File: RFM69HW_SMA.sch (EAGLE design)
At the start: 19 parts, among them U1 RFM69W, U2 MCP1701, X1 ANT

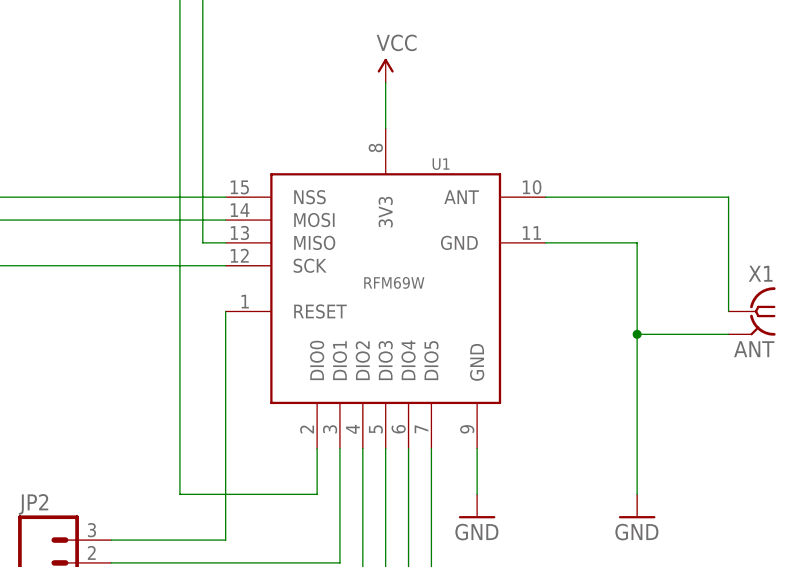
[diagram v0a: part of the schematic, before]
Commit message: Slight relayout
Re-layout. Break out all I/O pins. Use RFM69HW variant (same pinout).
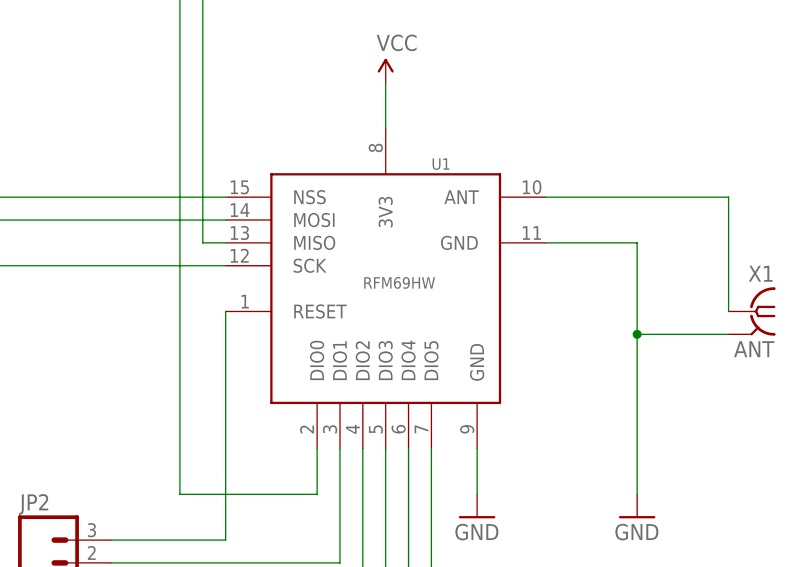
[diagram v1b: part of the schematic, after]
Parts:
- U1: value RFM69W -> RFM69HW; device ChipsParts:RFM69W -> custom_parts:RFM69HW
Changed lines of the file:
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@@
 <parts>
 <part name="FRAME1" library="SparkFun-Aesthetics" deviceset="FRAME-LETTER" device=""/>
-<part name="U1" library="ChipsParts" deviceset="RFM69W" device="" value="RFM69W"/>
+<part name="U1" library="custom_parts" deviceset="RFM69" device="HW" value="RFM69HW"/>
 <part name="U2" library="ChipsParts" deviceset="MCP1701" device=""/>
 <part name="JP1" library="SparkFun-Connectors" deviceset="M08" device="LONGPADS"/>

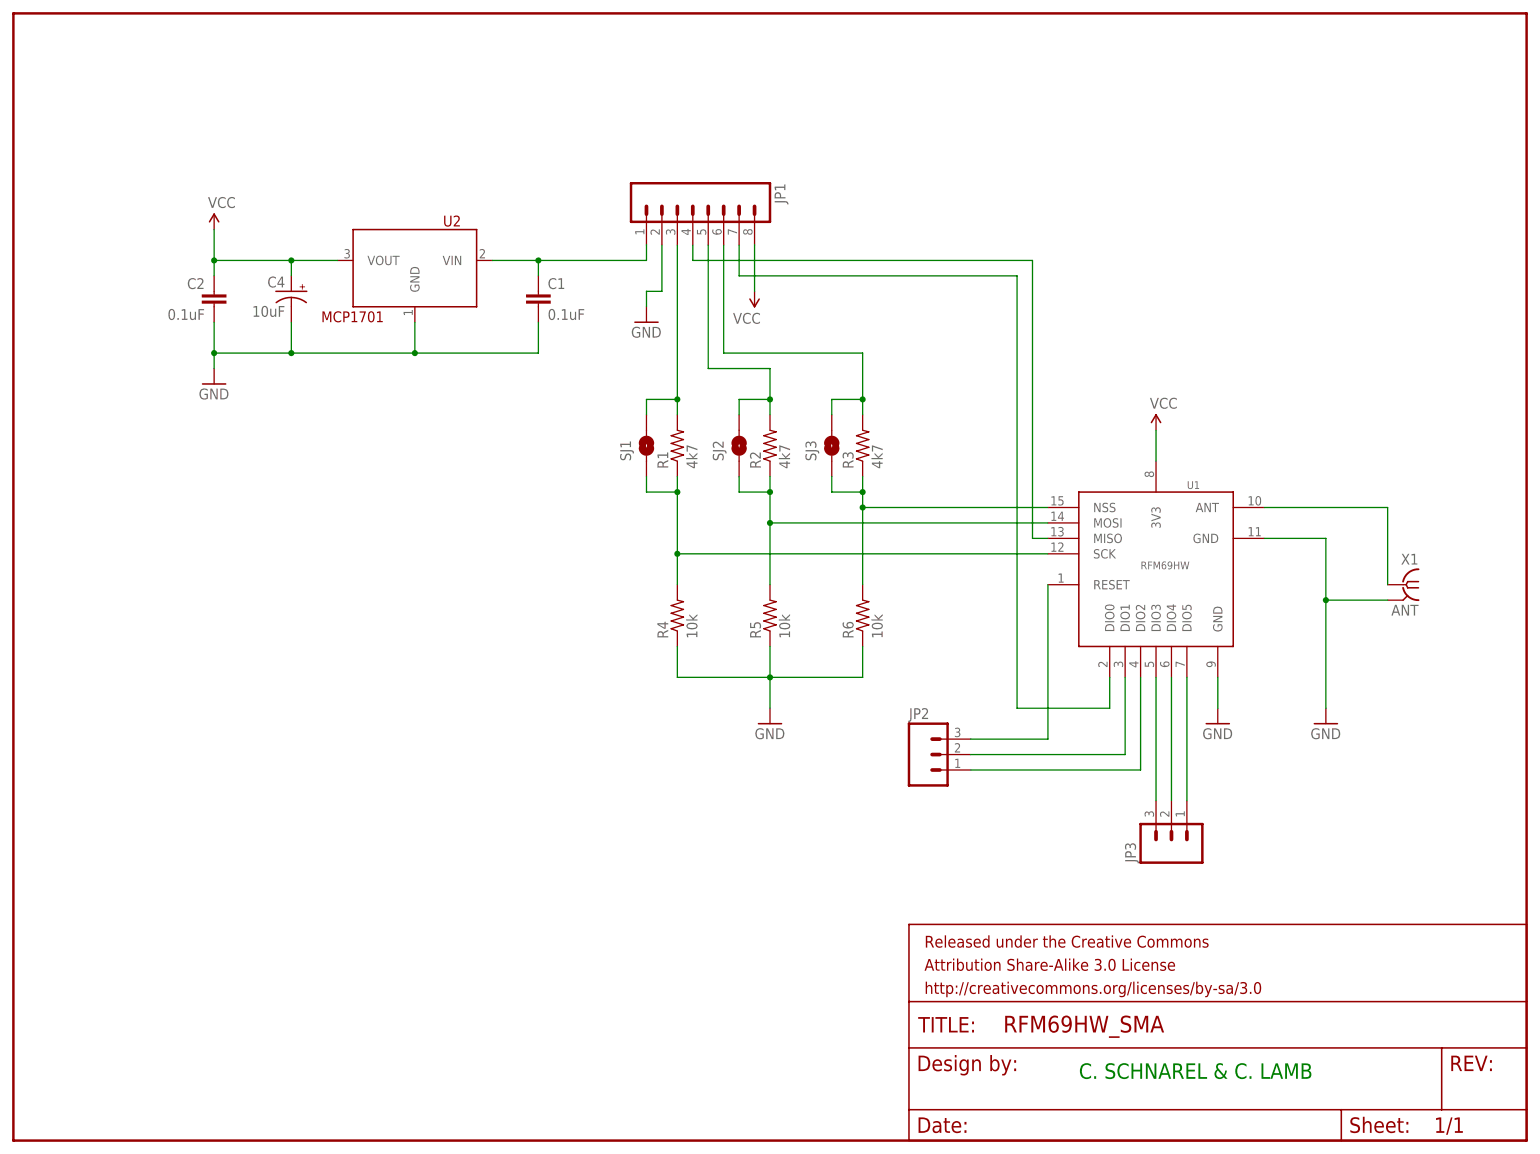
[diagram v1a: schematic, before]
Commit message: Update to remove JP2 and JP3
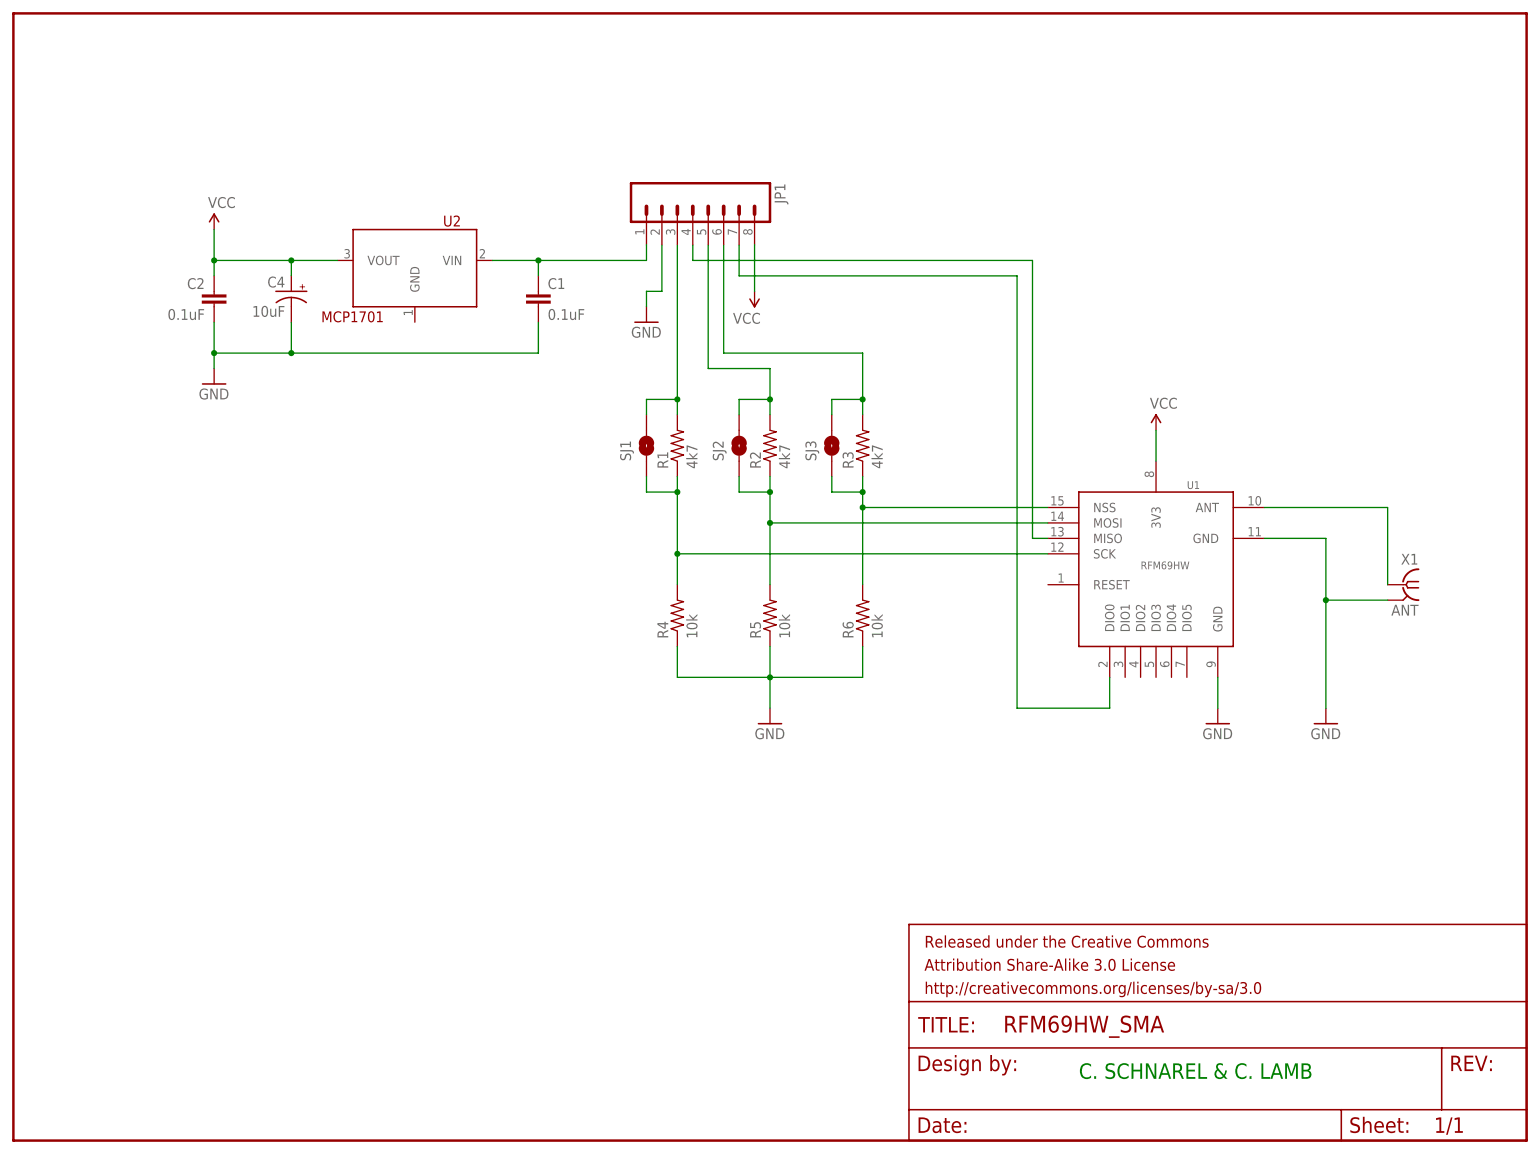
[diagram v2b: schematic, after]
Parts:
- removed JP2, JP3: (no value), SparkFun-Connectors:M03LOCK
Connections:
- removed net N$12: JP2.3, U1.RESET
- removed net N$13: JP2.2, U1.DIO1
- removed net N$14: JP2.1, U1.DIO2
- removed net N$15: JP3.1, U1.DIO5
- removed net N$16: JP3.2, U1.DIO4
- removed net N$17: JP3.3, U1.DIO3
- net GND: no longer U2.GND
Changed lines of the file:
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@@
 <classes>
 <class number="0" name="default" width="0" drill="0">
+<clearance class="0" value="0.3048"/>
 </class>
 </classes>
@@
 <part name="X1" library="custom_parts" deviceset="TE-SMA-JACK-STR" device="" value="ANT"/>
 <part name="GND5" library="SparkFun-Aesthetics" deviceset="GND" device=""/>
-<part name="JP2" library="SparkFun-Connectors" deviceset="M03" device="LOCK"/>
-<part name="JP3" library="SparkFun-Connectors" deviceset="M03" device="LOCK"/>
 </parts>
 <sheets>
@@
 <instance part="X1" gate="G$1" x="109.22" y="-10.16" rot="MR0"/>
 <instance part="GND5" gate="1" x="96.52" y="-33.02"/>
-<instance part="JP2" gate="G$1" x="30.48" y="-38.1"/>
-<instance part="JP3" gate="G$1" x="71.12" y="-53.34" rot="R90"/>
 </instances>
 <busses>
@@
 <wire x1="-86.36" y1="27.94" x2="-86.36" y2="25.4" width="0.1524" layer="91"/>
 <wire x1="-33.02" y1="33.02" x2="-33.02" y2="27.94" width="0.1524" layer="91"/>
-<wire x1="-33.02" y1="27.94" x2="-53.34" y2="27.94" width="0.1524" layer="91"/>
 <pinref part="C4" gate="G$1" pin="-"/>
-<wire x1="-53.34" y1="27.94" x2="-73.66" y2="27.94" width="0.1524" layer="91"/>
+<wire x1="-33.02" y1="27.94" x2="-73.66" y2="27.94" width="0.1524" layer="91"/>
 <wire x1="-73.66" y1="27.94" x2="-86.36" y2="27.94" width="0.1524" layer="91"/>
 <wire x1="-73.66" y1="33.02" x2="-73.66" y2="27.94" width="0.1524" layer="91"/>
-<pinref part="U2" gate="G$1" pin="GND"/>
-<wire x1="-53.34" y1="33.02" x2="-53.34" y2="27.94" width="0.1524" layer="91"/>
-<junction x="-53.34" y="27.94"/>
 <junction x="-73.66" y="27.94"/>
 <junction x="-86.36" y="27.94"/>
@@
 </segment>
 </net>
-<net name="N$13" class="0">
-<segment>
-<pinref part="JP2" gate="G$1" pin="2"/>
-<pinref part="U1" gate="G$1" pin="DIO1"/>
-<wire x1="38.1" y1="-38.1" x2="63.5" y2="-38.1" width="0.1524" layer="91"/>
-<wire x1="63.5" y1="-38.1" x2="63.5" y2="-25.4" width="0.1524" layer="91"/>
-</segment>
-</net>
-<net name="N$14" class="0">
-<segment>
-<pinref part="JP2" gate="G$1" pin="1"/>
-<pinref part="U1" gate="G$1" pin="DIO2"/>
-<wire x1="38.1" y1="-40.64" x2="66.04" y2="-40.64" width="0.1524" layer="91"/>
-<wire x1="66.04" y1="-40.64" x2="66.04" y2="-25.4" width="0.1524" layer="91"/>
-</segment>
-</net>
-<net name="N$15" class="0">
-<segment>
-<pinref part="U1" gate="G$1" pin="DIO5"/>
-<pinref part="JP3" gate="G$1" pin="1"/>
-<wire x1="73.66" y1="-25.4" x2="73.66" y2="-45.72" width="0.1524" layer="91"/>
-</segment>
-</net>
-<net name="N$16" class="0">
-<segment>
-<pinref part="U1" gate="G$1" pin="DIO4"/>
-<pinref part="JP3" gate="G$1" pin="2"/>
-<wire x1="71.12" y1="-25.4" x2="71.12" y2="-45.72" width="0.1524" layer="91"/>
-</segment>
-</net>
-<net name="N$17" class="0">
-<segment>
-<pinref part="U1" gate="G$1" pin="DIO3"/>
-<pinref part="JP3" gate="G$1" pin="3"/>
-<wire x1="68.58" y1="-25.4" x2="68.58" y2="-45.72" width="0.1524" layer="91"/>
-</segment>
-</net>
-<net name="N$12" class="0">
-<segment>
-<pinref part="JP2" gate="G$1" pin="3"/>
-<pinref part="U1" gate="G$1" pin="RESET"/>
-<wire x1="38.1" y1="-35.56" x2="50.8" y2="-35.56" width="0.1524" layer="91"/>
-<wire x1="50.8" y1="-35.56" x2="50.8" y2="-10.16" width="0.1524" layer="91"/>
-</segment>
-</net>
